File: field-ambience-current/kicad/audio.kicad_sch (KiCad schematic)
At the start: 22 parts, among them J6 Speaker L (PUI AS04008PS, 4R 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, J7 Speaker R (PUI AS04008PS, 4R 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, U3 PCM5102A I²S DAC (TSSOP-20), U4 PAM8403H Class-D Stereo Amp (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

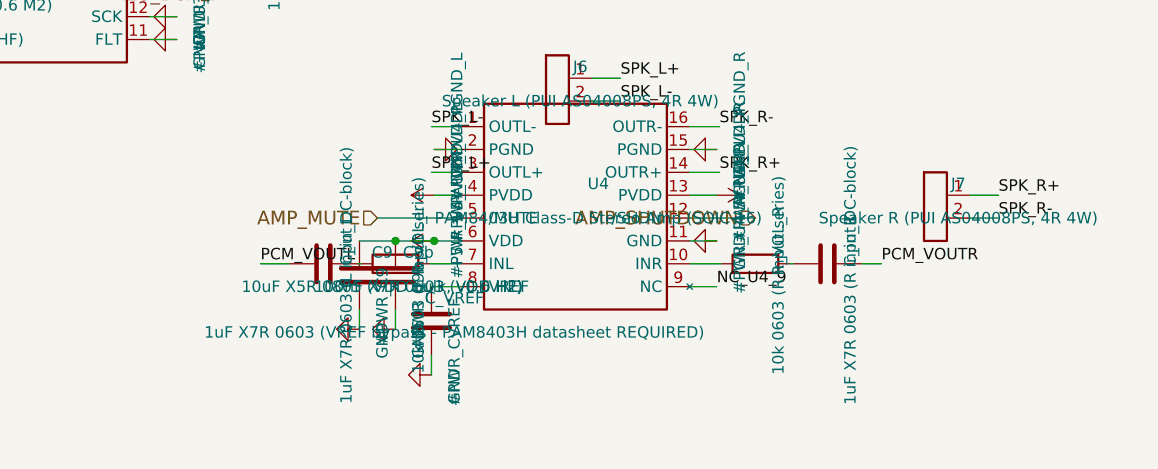
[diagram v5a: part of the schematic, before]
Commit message: v0.6.3-r2: PAM8403 SHDN/MUTE pull-downs + UART naming + TODO list
Addresses 2nd-iteration ChatGPT review findings (most that don't need
KiCad GUI). All TODO items documented in PCB_TODO.md.

B4: PAM8403H /SHDN and /MUTE hardware pull-downs
- R_MUTE_PD 10k from pin 5 (/MUTE) to GND
- R_SHDN_PD 10k from pin 12 (/SHDN) to GND
- Default state during Pico boot/reset = both LOW = Amp OFF + MUTED
- Pico firmware drives HIGH only after power-sequencing per SPEC §5
- Prevents undefined Amp state during boot transients (pop/click safety)

I7: UART net naming disambiguated
- Old: UART0_TX / UART0_RX (perspective-ambiguous)
- New:
  - PICO_TX_PI_RX (Pico GP0 → Pi GPIO15 pin 10)
  - PI_TX_PICO_RX (Pi GPIO14 pin 8 → R1 1k → Pico GP1)
- Changed in pico_sheet, pi_sheet, root_sheet (pins + labels)

N4: Titleblock revs synced
- audio.kicad_sch: v0.6.1 → v0.6.3
- power_tree.kicad_sch: v0.6 → v0.6.3
- Comments updated to reflect current state

N5: Stale comments cleanup
- power_tree_sheet: USB-C pin-number references updated to USB-C spec
- audio_sheet: PAM8403 references updated to PAM8403H + PDF reference
- BLOCKER-comment in audio sheet replaced with "boot-safe pull-downs added"

New PCB_TODO.md tracks remaining items for PCB-layout readiness:
- BLOCKER (4): need KiCad GUI — footprint verification, ERC report
- IMPORTANT (7): power budget recalc, mech coords, BOM split, etc.
- NICE-TO-HAVE (5): XSMT via GPIO, I²S series R, etc.

Analyzer status: 0 functional errors (same 3 VM-001 false positives),
19 warnings, 87 components (was 85, +2 for pull-downs), 117 nets.

Verified via analyzer pin_nets:
- R_MUTE_PD: pin1=AMP_MUTE, pin2=GND ✓
- R_SHDN_PD: pin1=AMP_SHUTDOWN, pin2=GND ✓
- U1 Pin 1 (GP0) = PICO_TX_PI_RX ✓
- U1 Pin 2 (GP1) = PI_TX_PICO_RX ✓
- U4 Pin 5 (MUTE) = AMP_MUTE ✓
- U4 Pin 12 (SHDN) = AMP_SHUTDOWN ✓

Note on reviewer's USB-C claim: Reviewer indicated USB-C symbol still
has wrong pinout in PR. Verified via GitHub API that PR HEAD (commit
5ca0bcb) has the correct mapping (VB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
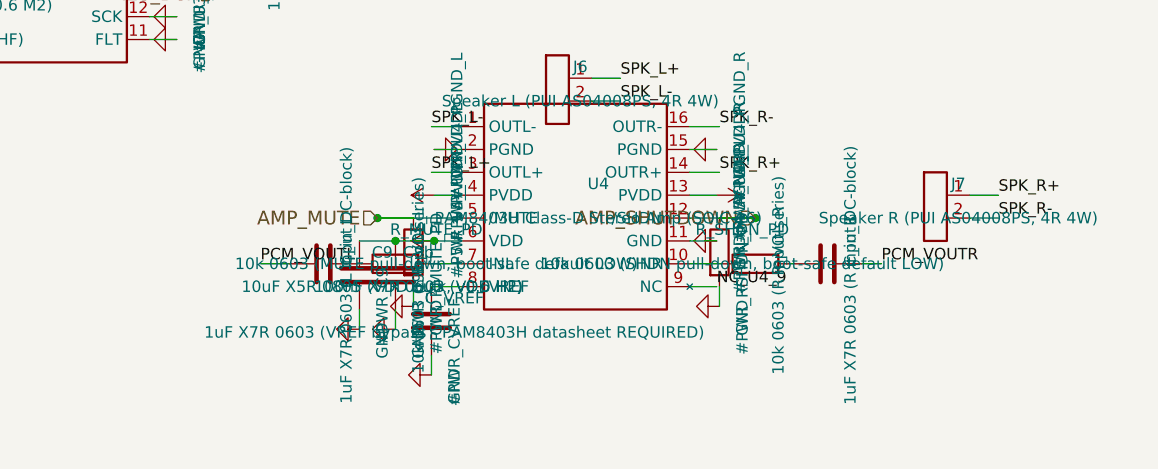
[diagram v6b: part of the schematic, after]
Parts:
- added R_MUTE_PD: 10k 0603 (MUTE pull-down, boot-safe default LOW), Resistor_SMD:R_0603_1608Metric, symbol Device:R
- added R_SHDN_PD: 10k 0603 (SHDN pull-down, boot-safe default LOW), Resistor_SMD:R_0603_1608Metric, symbol Device:R
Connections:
- net AMP_MUTE: now also R_MUTE_PD.1
- net AMP_SHUTDOWN: now also R_SHDN_PD.1
- net GND: now also R_MUTE_PD.2, R_SHDN_PD.2
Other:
- title: Field Ambience PCB — Sheet 6: Audio (PCM5102A + PAM8403) -> Field Ambience PCB — Sheet 6: Audio (PCM5102A + PAM8403H)
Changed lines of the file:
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@@
   (paper "A3")
   (title_block
-    (title "Field Ambience PCB — Sheet 6: Audio (PCM5102A + PAM8403)")
-    (date "2026-05-13")
-    (rev "0.6.1")
+    (title "Field Ambience PCB — Sheet 6: Audio (PCM5102A + PAM8403H)")
+    (date "2026-05-14")
+    (rev "0.6.3")
     (company "Field Ambience Project")
-    (comment 1 "Per SPEC v0.6 §8 + Fixes H2/M2/C2 + REVIEW PIN-FIX")
+    (comment 1 "Per SPEC v0.6.3 §8 + Errata-Fixes (PCM5102A TI, PAM8403H PDF verifiziert)")
     (comment 2 "PCM5102A pinout per TI SLAS859C: CPVDD=1, OUTL=6, AVDD=8, BCK=13, DIN=14, LRCK=15, DVDD=20")
-    (comment 3 "PAM8403 pinout per Diodes Inc DS31295 (LCSC C17337 = PAM8403DR-H)")
-    (comment 4 "BLOCKER: PAM8403 PVDD/PGND-Pairs (4/2, 10/12) MUESSEN gegen PAM8403DR-H Datasheet verifiziert werden vor PCB-Layout"))
+    (comment 3 "PAM8403H pinout per Diodes Inc PAM8403H.PDF Rev 1-0 (LCSC C17337)")
+    (comment 4 "v0.6.3 adds R_MUTE_PD + R_SHDN_PD 10k pull-downs - Amp default-OFF/muted during Pico boot"))
   (symbol (lib_id "Audio:PCM5102A") (at 100.0 100.0 0) (unit 1)
     (in_bom yes) (on_board yes) (dnp no)
@@
       (project "field_ambience"
         (path "/66fcdc89-be06-4d61-a855-abf9641d963c" (reference "#PWR_U4_PVDDL") (unit 1)))))
+  (symbol (lib_id "Device:R") (at 142 135.08 0) (unit 1)
+    (in_bom yes) (on_board yes) (dnp no)
+      (property "Reference" "R_MUTE_PD" (at 144.54 132.54000000000002 0)
+        (effects (font (size 1.27 1.27))))
+      (property "Value" "10k 0603 (MUTE pull-down, boot-safe default LOW)" (at 144.54 136.35000000000002 0)
+        (effects (font (size 1.27 1.27))))
+      (property "Footprint" "Resistor_SMD:R_0603_1608Metric" (at 142 135.08 0)
+        (effects (font (size 1.27 1.27)) hide))
+      (property "Datasheet" "~" (at 142 135.08 0)
+        (effects (font (size 1.27 1.27)) hide))
+      (property "MPN" "RC0603FR-0710KL" (at 144.54 138.89000000000001 0)
+        (effects (font (size 1.27 1.27)) hide))
+      (property "LCSC" "C25804" (at 144.54 140.16000000000003 0)
+        (effects (font (size 1.27 1.27)) hide))
+    (instances
+      (project "field_ambience"
+        (path "/66fcdc89-be06-4d61-a855-abf9641d963c" (reference "R_MUTE_PD") (unit 1)))))
+  (symbol (lib_id "Power:GND") (at 142 141.08 270) (unit 1)
+    (in_bom yes) (on_board yes) (dnp no)
+      (property "Reference" "#PWR_RMUTE_PD" (at 144.54 138.54000000000002 0)
+        (effects (font (size 1.27 1.27))))
+      (property "Value" "GND" (at 144.54 142.35000000000002 0)
+        (effects (font (size 1.27 1.27))))
+      (property "Footprint" "" (at 142 141.08 0)
+        (effects (font (size 1.27 1.27)) hide))
+      (property "Datasheet" "~" (at 142 141.08 0)
+        (effects (font (size 1.27 1.27)) hide))
+    (instances
+      (project "field_ambience"
+        (path "/66fcdc89-be06-4d61-a855-abf9641d963c" (reference "#PWR_RMUTE_PD") (unit 1)))))
   (symbol (lib_id "Power:+5V") (at 144.3 133.81 90) (unit 1)
     (in_bom yes) (on_board yes) (dnp no)
@@
       (project "field_ambience"
         (path "/66fcdc89-be06-4d61-a855-abf9641d963c" (reference "#PWR_U4_AGND_R") (unit 1)))))
+  (symbol (lib_id "Device:R") (at 176 135.08 0) (unit 1)
+    (in_bom yes) (on_board yes) (dnp no)
+      (property "Reference" "R_SHDN_PD" (at 178.54 132.54000000000002 0)
+        (effects (font (size 1.27 1.27))))
+      (property "Value" "10k 0603 (SHDN pull-down, boot-safe default LOW)" (at 178.54 136.35000000000002 0)
+        (effects (font (size 1.27 1.27))))
+      (property "Footprint" "Resistor_SMD:R_0603_1608Metric" (at 176 135.08 0)
+        (effects (font (size 1.27 1.27)) hide))
+      (property "Datasheet" "~" (at 176 135.08 0)
+        (effects (font (size 1.27 1.27)) hide))
+      (property "MPN" "RC0603FR-0710KL" (at 178.54 138.89000000000001 0)
+        (effects (font (size 1.27 1.27)) hide))
+      (property "LCSC" "C25804" (at 178.54 140.16000000000003 0)
+        (effects (font (size 1.27 1.27)) hide))
+    (instances
+      (project "field_ambience"
+        (path "/66fcdc89-be06-4d61-a855-abf9641d963c" (reference "R_SHDN_PD") (unit 1)))))
+  (symbol (lib_id "Power:GND") (at 176 141.08 270) (unit 1)
+    (in_bom yes) (on_board yes) (dnp no)
+      (property "Reference" "#PWR_RSHDN_PD" (at 178.54 138.54000000000002 0)
+        (effects (font (size 1.27 1.27))))
+      (property "Value" "GND" (at 178.54 142.35000000000002 0)
+        (effects (font (size 1.27 1.27))))
+      (property "Footprint" "" (at 176 141.08 0)
+        (effects (font (size 1.27 1.27)) hide))
+      (property "Datasheet" "~" (at 176 141.08 0)
+        (effects (font (size 1.27 1.27)) hide))
+    (instances
+      (project "field_ambience"
+        (path "/66fcdc89-be06-4d61-a855-abf9641d963c" (reference "#PWR_RSHDN_PD") (unit 1)))))
   (symbol (lib_id "Power:+5V") (at 175.7 128.73 270) (unit 1)
     (in_bom yes) (on_board yes) (dnp no)
@@
     (stroke (width 0) (type default))
 )
+  (wire (pts (xy 138 131.27) (xy 142 131.27))
+    (stroke (width 0) (type default))
+)
+  (wire (pts (xy 142 138.89000000000001) (xy 142 141.08))
+    (stroke (width 0) (type default))
+)
   (wire (pts (xy 147.3 133.81) (xy 144.3 133.81))
     (stroke (width 0) (type default))
@@
     (stroke (width 0) (type default))
 )
+  (wire (pts (xy 180 131.27) (xy 176 131.27))
+    (stroke (width 0) (type default))
+)
+  (wire (pts (xy 176 138.89000000000001) (xy 176 141.08))
+    (stroke (width 0) (type default))
+)
   (wire (pts (xy 172.7 128.73) (xy 175.7 128.73))
     (stroke (width 0) (type default))
@@
   (junction (at 120 88.57) (diameter 0) (color 0 0 0 0)
 )
+  (junction (at 138 131.27) (diameter 0) (color 0 0 0 0)
+)
   (junction (at 144.3 133.81) (diameter 0) (color 0 0 0 0)
 )
   (junction (at 140 133.81) (diameter 0) (color 0 0 0 0)
 )
+  (junction (at 180 131.27) (diameter 0) (color 0 0 0 0)
+)
   (label "PCM_VOUTL" (at 80 101.27 0) (fields_autoplaced)

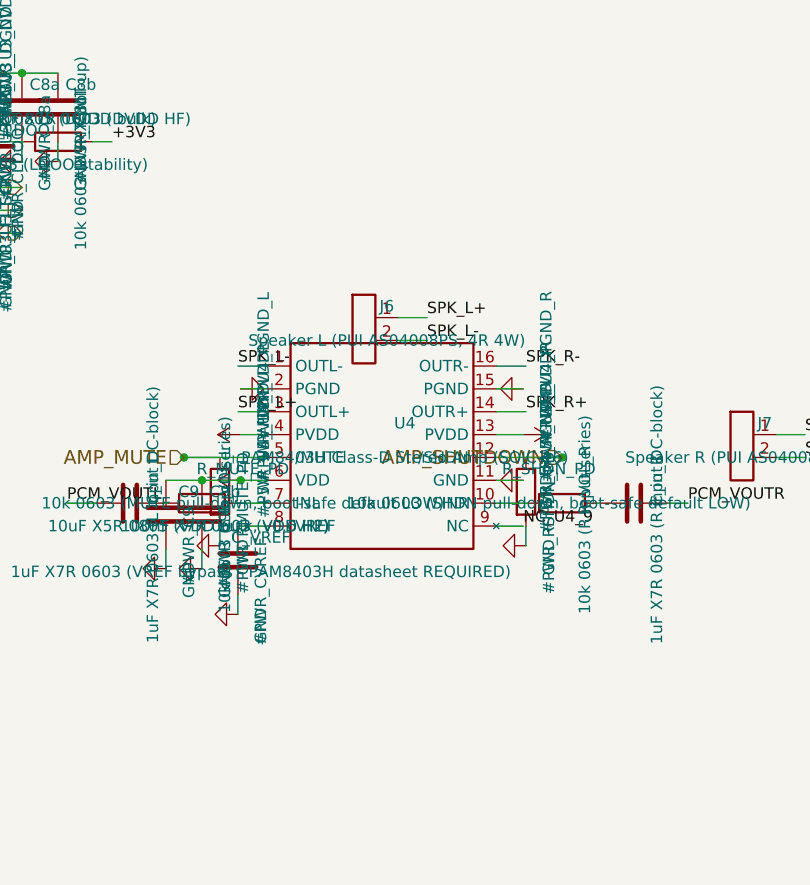
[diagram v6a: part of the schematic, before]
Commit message: v0.6.3-r4: SPEC body cleanup + audio gain fix (R_VOL 10k→20k)
Addresses 3rd-round ChatGPT review: spec internal inconsistencies +
real audio clipping risk.

Audio fix — R_VOL_L/R 10kΩ → 20kΩ:
- PAM8403H datasheet (DS31295): RI minimum = 18 kΩ for spec'd 24 dB gain.
- With RI = 10kΩ: AVD = 2*142k/10k = 28.4 = 29 dB (exceeds spec, more
  clipping headroom needed in firmware).
- With RI = 20kΩ: AVD = 2*142k/20k = 14.2 = 23 dB (within datasheet spec).
- LCSC C25092 (RC0603FR-0720KL) instead of C25804 (10kΩ).

SPEC body section cleanup (was contradicting v0.6.3-r3 errata):
- §3 Power Budget: 1.405A peak (old, optimistic) → 2.48A realistic table
- §3 USB-C Power Delivery: "5.1k = 3A capable" (wrong) → Variante A
  (Firmware Volume-Clamp) für Prototyp, TPS25750 for product
- §3 Polyfuse rationale: re-justified with new budget + firmware-clamp
  assumption
- §3 C_BULK MPN: Nichicon PCV1A102MCL1GS polymer (low-ESR, defined Inrush)
- §4 BOM header: "Full PCBA" wording removed → "gesplittet in Section
  A/B/C"; LCSC numbers explicitly normalized in header note
- §8 Audio Path: PCM5102A pin numbers from TI datasheet (CPVDD=1, OUTL=6,
  AVDD=8, DVDD=20). VCOM marked as NOT-A-PIN (was misleading in v0.6).
- §8 NEW: "Audio-Gain-Strategy" subsection documenting the 2.1Vrms PCM →
  PAM8403 clipping risk, R_VOL=20k decision, firmware ≤-24dB requirement.
- §8 PAM8403 connection table updated with all 16 pins per Diodes
  DS31295 + v0.6.3-r2 pull-downs noted
- §10 Risks: marked v0.6.3-r3 items as resolved; added blockers B1/B2/B3
  pointer to PCB_TODO.md
- §11 Next Steps: reordered to reflect current "schematic done, layout
  pending" state with new blocker list

Analyzer: 0 errors, 19 warnings, 3 VM-001 false-positives.
90 components, 120 nets (unchanged from r3).

Remaining BLOCKERS (still require KiCad GUI locally):
- B1 PAM8403H SOIC-16 footprint pad-mapping
- B2 USB-C TYPE-C-31-M-12 footprint pad-mapping
- B3 KiCad GUI ERC + report under reports/

Reviewer's "single source of trut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
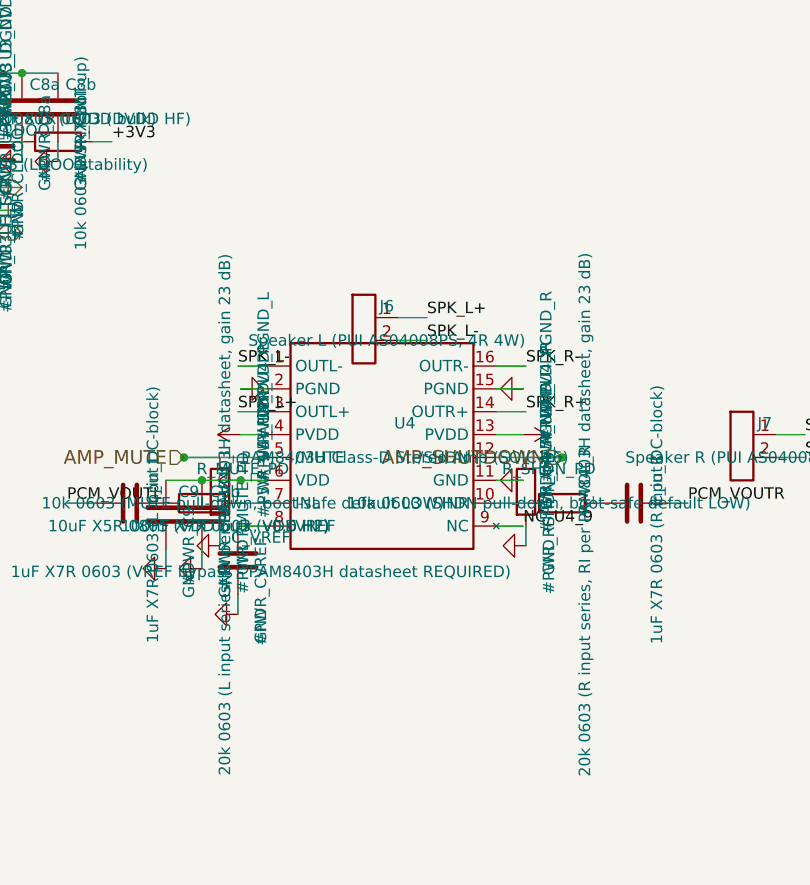
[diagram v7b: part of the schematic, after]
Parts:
- R_VOL_L: value 10k 0603 (L input series) -> 20k 0603 (L input series, RI per PAM8403H datasheet, gain 23 dB); LCSC C25804 -> C25092; MPN RC0603FR-0710KL -> RC0603FR-0720KL
- R_VOL_R: value 10k 0603 (R input series) -> 20k 0603 (R input series, RI per PAM8403H datasheet, gain 23 dB); LCSC C25804 -> C25092; MPN RC0603FR-0710KL -> RC0603FR-0720KL
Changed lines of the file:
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@@
       (property "Reference" "R_VOL_L" (at 142.54 133.81 0)
         (effects (font (size 1.27 1.27))))
-      (property "Value" "10k 0603 (L input series)" (at 142.54 137.62 0)
+      (property "Value" "20k 0603 (L input series, RI per PAM8403H datasheet, gain 23 dB)" (at 142.54 137.62 0)
         (effects (font (size 1.27 1.27))))
       (property "Footprint" "Resistor_SMD:R_0603_1608Metric" (at 140 136.35 0)
@@
       (property "Datasheet" "~" (at 140 136.35 0)
         (effects (font (size 1.27 1.27)) hide))
-      (property "MPN" "RC0603FR-0710KL" (at 142.54 140.16 0)
+      (property "MPN" "RC0603FR-0720KL" (at 142.54 140.16 0)
         (effects (font (size 1.27 1.27)) hide))
-      (property "LCSC" "C25804" (at 142.54 141.43 0)
+      (property "LCSC" "C25092" (at 142.54 141.43 0)
         (effects (font (size 1.27 1.27)) hide))
     (instances
@@
       (property "Reference" "R_VOL_R" (at 182.54 133.81 0)
         (effects (font (size 1.27 1.27))))
-      (property "Value" "10k 0603 (R input series)" (at 182.54 137.62 0)
+      (property "Value" "20k 0603 (R input series, RI per PAM8403H datasheet, gain 23 dB)" (at 182.54 137.62 0)
         (effects (font (size 1.27 1.27))))
       (property "Footprint" "Resistor_SMD:R_0603_1608Metric" (at 180 136.35 0)
@@
       (property "Datasheet" "~" (at 180 136.35 0)
         (effects (font (size 1.27 1.27)) hide))
-      (property "MPN" "RC0603FR-0710KL" (at 182.54 140.16 0)
+      (property "MPN" "RC0603FR-0720KL" (at 182.54 140.16 0)
         (effects (font (size 1.27 1.27)) hide))
-      (property "LCSC" "C25804" (at 182.54 141.43 0)
+      (property "LCSC" "C25092" (at 182.54 141.43 0)
         (effects (font (size 1.27 1.27)) hide))
     (instances
